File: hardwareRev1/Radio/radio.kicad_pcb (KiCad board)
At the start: 4 copper layers, 37 x 24.5 mm, 61 parts, among them J1 SMA, U1 AX503, U2 PE42424, U3 RF5110G, X1 TCXO

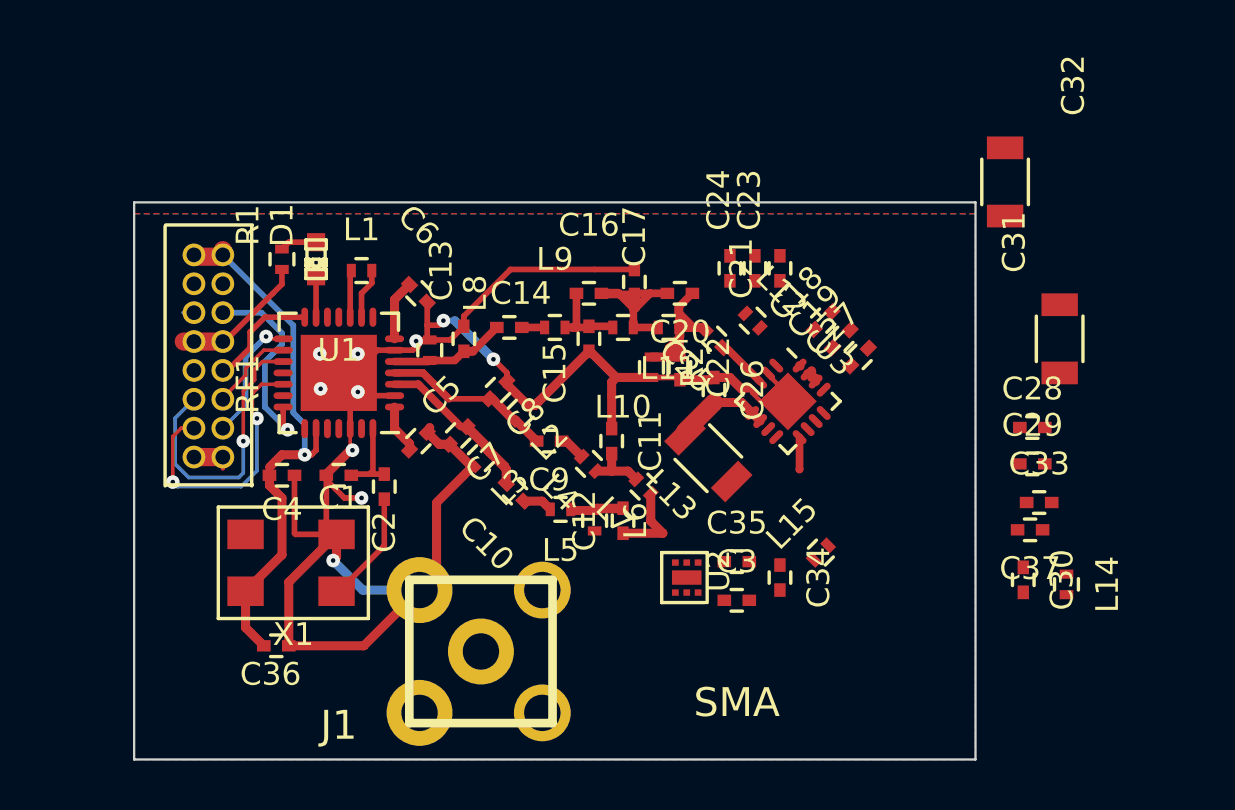
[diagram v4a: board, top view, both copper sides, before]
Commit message: Made the board 4 layer.
Added a MCU to theback...
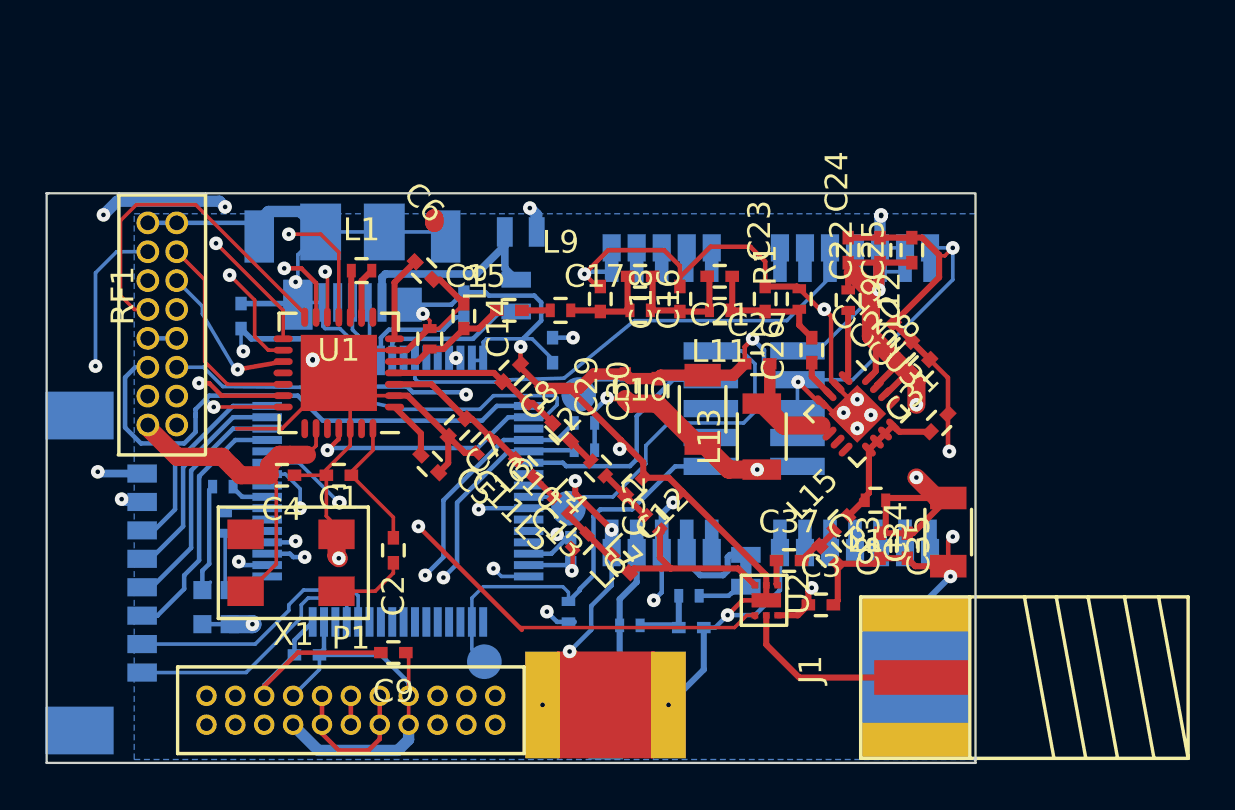
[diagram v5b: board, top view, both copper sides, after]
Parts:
- added C38: C, Capacitors_SMD:C_0402, B.Cu at (81.5, 57.0)
- added C39: C, Capacitors_SMD:C_0402, B.Cu at (71.7, 57.5)
- added C40: C, Capacitors_SMD:C_0402, B.Cu at (74.6, 72.4)
- added C41: C, Capacitors_SMD:C_0402, B.Cu at (86.2, 67.8)
- added C42: C, Capacitors_SMD:C_0402, B.Cu at (85.4, 59.0)
- added C43: 47pF, Capacitors_SMD:C_0402, B.Cu at (91.5, 71.2)
- added D2: LED, LEDs:LED-0603, B.Cu at (71.2, 70.3)
- added J2: edgeMountSMA, hardwareRev1:EdgeSMA, B.Cu at (90.5, 78.6)
- added JMP2: SJMPClosed, SMDJMP-CLOSED, B.Cu at (93.9, 68.7)
- added JMP3: SJMPOpen, hardwareRev1:SMDJMP-OPEN, B.Cu at (84.0, 53.8)
- added JMP4: SJMPOpen, hardwareRev1:SMDJMP-OPEN, B.Cu at (83.8, 56.6)
- added L16: 27nH, Resistors_SMD:R_0402, B.Cu at (88.8, 71.1)
- added P1: CONN_11X2, hardwareRev1:1.27mmPitchHeader11X2, F.Cu at (77.8, 74.2)
- added P2: CONN_1, Measurement_Points:Measurement_Point_Round-SMD-Pad_Small, B.Cu at (86.1, 66.0)
- added P3: CONN_8, Connectors_Molex:Connector_Molex_PicoBlade_53398-0871, B.Cu at (64.6, 68.8)
- added P4: CONN_5X2, hardwareRev1:CortexDebug, B.Cu at (94.9, 60.3)
- added P5: CONN_1, Measurement_Points:Measurement_Point_Round-SMD-Pad_Small, B.Cu at (86.5, 61.0)
- added P6: CONN_1, Measurement_Points:Measurement_Point_Round-SMD-Pad_Small, B.Cu at (82.4, 72.7)
- added R3: R, Resistors_SMD:R_0402, B.Cu at (86.8, 62.2)
- added R4: R, Resistors_SMD:R_0402, B.Cu at (70.9, 65.0)
- added R5: R, Resistors_SMD:R_0402, B.Cu at (71.0, 66.6)
- added R6: R, Resistors_SMD:R_0402, B.Cu at (86.1, 70.5)
- added R7: 10, Resistors_SMD:R_0402, B.Cu at (91.4, 69.8)
- added RF2: NEO7, NEO-7, B.Cu at (87.0, 54.5)
- added U4: MKL26Z128VLH4, w_smd_lqfp:lqfp64, B.Cu at (78.6, 65.2)
- added U6: MICRO-B_USB, USB:USB micro-female, B.Cu at (76.6, 54.0)
- C11: value 12pf -> 10pf
- C13: value 2.2pf -> 12pf
- C14: value 22pf -> 2.2pf
- C15: value 33pf -> 22pf
- C16: value 4.7pf -> 33pf
- C17: value 47pf -> 4.7pf
- C18: value 10nf -> 47pf
- C19: value 1nf -> 10nf
- C20: value 1.8pf -> 1nf
- C21: value 10nf -> 1.8pf
- C22: value 15pf -> 10nf
- C23: value 1nf -> 15pf
- C24: value 27pf -> 1nf
- C25: value 100pf -> 27pf
- C26: value 27pf -> 100pf
- C27: value 47pf -> 27pf
- C28: value 1nf -> 47pf
- C29: value 10nf -> 1nf
- C30: value 33pf -> 10nf
- C31: value 3.3uf -> 33pf; footprint Capacitors_SMD:C_1206 -> Capacitors_SMD:C_0402
- C33: value 1nf -> C
- C34: value 56pf -> 3.3uf; footprint Capacitors_SMD:C_0402 -> Capacitors_SMD:C_1206
- C35: value 100pf -> 1nf
- C36: value 100pf -> 56pf
- C37: value C -> 100pf
- C9: value 10pf -> 100pf
- D1: moved to B.Cu
- J1: value SMA -> edgeMountSMA; footprint hardwareRev1:SMA -> hardwareRev1:EdgeSMA
- R1: value R -> 180
- R2: value 180 -> R; moved to B.Cu
- RF1: footprint 1.27mm2X8 -> hardwareRev1:1.27mm2X8
- U2: footprint PE4242 -> hardwareRev1:PE4242
- X1: footprint FOX924B -> hardwareRev1:FOX924B
- moved C36 24.6 mm to (97.5, 68.0), turned to 315 degrees
- moved J1 23.4 mm to (105.3, 76.2), turned to 90 degrees
- moved R1 22.8 mm to (96.2, 56.8)
- moved C29 18.2 mm to (88.6, 60.6), turned to 90 degrees
- moved C30 18.1 mm to (90.0, 60.8), turned to 90 degrees
- moved C32 16.6 mm to (92.0, 61.6), turned to 90 degrees
- moved D1 16.1 mm to (70.0, 70.3), turned to 270 degrees
- moved C13 12.1 mm to (88.4, 68.4), turned to 135 degrees
- moved C9 11.6 mm to (78.4, 72.3)
- moved RF1 10.8 mm to (67.6, 53.4), turned to 180 degrees
- moved C37 10.7 mm to (95.8, 68.2), turned to 0 degrees
- moved C22 10.2 mm to (99.8, 54.6), turned to 90 degrees
- moved C20 10.1 mm to (100.8, 59.0), turned to 45 degrees
- moved C25 9.53 mm to (101.2, 54.6), turned to 90 degrees
- moved L14 9.18 mm to (99.6, 65.6), turned to 180 degrees
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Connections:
- C11 pad 1: GND -> Net-(C11-Pad1)
- C12 pad 1: Net-(C12-Pad1) -> GND
- C13 pad 1: /PA/PAInput -> Net-(C13-Pad1)
- C13 pad 2: GND -> Net-(C13-Pad2)
- C14 pad 1: Net-(C14-Pad1) -> /PA/PAInput
- C14 pad 2: /PA/PAInput -> GND
- C15 pad 2: GND -> /PA/PAInput
- C16 pad 2: Net-(C15-Pad1) -> GND
- C17 pad 1: Net-(C16-Pad1) -> Net-(C17-Pad1)
- C17 pad 2: GND -> Net-(C16-Pad1)
- C18 pad 1: +3.3V -> Net-(C17-Pad1)
- C20 pad 1: Net-(C20-Pad1) -> +3.3V
- C20 pad 2: Net-(C16-Pad1) -> GND
- C21 pad 1: +3.3V -> Net-(C21-Pad1)
- C21 pad 2: GND -> Net-(C17-Pad1)
- C22 pad 1: Net-(C20-Pad1) -> +3.3V
- C23 pad 1: +3.3V -> Net-(C21-Pad1)
- C25 pad 1: Net-(C25-Pad1) -> +3.3V
- C25 pad 2: Net-(C20-Pad1) -> GND
- C26 pad 1: GND -> Net-(C26-Pad1)
- C26 pad 2: Net-(C26-Pad2) -> Net-(C21-Pad1)
- C27 pad 1: +3.3V -> GND
- C27 pad 2: GND -> Net-(C27-Pad2)
- C30 pad 1: Net-(C30-Pad1) -> +3.3V
- C31 pad 1: +3.3V -> Net-(C31-Pad1)
- C32 pad 1: GND -> +3.3V
- C32 pad 2: +3.3V -> GND
- C33 pad 1: +3.3V -> GND
- C33 pad 2: GND -> +3.3V
- C34 pad 1: Net-(C34-Pad1) -> GND
- C34 pad 2: GND -> +3.3V
- C35 pad 1: /PA/PAOutput -> +3.3V
- C35 pad 2: Net-(C34-Pad1) -> GND
- C36 pad 1: GND -> Net-(C36-Pad1)
- C36 pad 2: +3.3V -> GND
- C37 pad 1: GND -> /PA/PAOutput
- C37 pad 2: +3.3V -> Net-(C36-Pad1)
- C7 pad 1: Net-(C10-Pad2) -> Net-(C11-Pad2)
- C8 pad 2: Net-(C8-Pad2) -> Net-(C10-Pad2)
- C9 pad 1: Net-(C9-Pad1) -> GND
- C9 pad 2: Net-(C8-Pad2) -> +3.3V
- D1 pad 2: Net-(D1-Pad2) -> GND
- L10 pad 1: Net-(C16-Pad1) -> Net-(C17-Pad1)
- L10 pad 2: Net-(C15-Pad1) -> Net-(C16-Pad1)
- L11 pad 1: Net-(C20-Pad1) -> Net-(C21-Pad1)
- L11 pad 2: Net-(C16-Pad1) -> Net-(C17-Pad1)
- L13 pad 2: Net-(C26-Pad2) -> Net-(C27-Pad2)
- L14 pad 2: Net-(C30-Pad1) -> Net-(C31-Pad1)
- L15 pad 1: Net-(C34-Pad1) -> Net-(C36-Pad1)
- L15 pad 2: Net-(C30-Pad1) -> Net-(C31-Pad1)
- L2 pad 2: Net-(C8-Pad2) -> Net-(C10-Pad2)
- L3 pad 1: Net-(C10-Pad2) -> Net-(C11-Pad2)
- L4 pad 1: Net-(C11-Pad2) -> Net-(C12-Pad2)
- L4 pad 2: Net-(C9-Pad1) -> Net-(C10-Pad1)
- L5 pad 1: Net-(C12-Pad2) -> Net-(C13-Pad2)
- L5 pad 2: Net-(C10-Pad1) -> Net-(C11-Pad1)
- L6 pad 1: Net-(C12-Pad2) -> Net-(C13-Pad2)
- L7 pad 1: Net-(C12-Pad1) -> Net-(C13-Pad1)
- L7 pad 2: Net-(C11-Pad2) -> Net-(C12-Pad2)
- L9 pad 1: Net-(C15-Pad1) -> Net-(C16-Pad1)
- L9 pad 2: Net-(C14-Pad1) -> Net-(C15-Pad1)
- R1 pad 1: GND -> Net-(C21-Pad1)
- R1 pad 2: Net-(D1-Pad2) -> GND
- R2 pad 1: Net-(C20-Pad1) -> +3.3V
- R2 pad 2: GND -> /internalI2C0SDA
- U1 pad 12: (no net) -> /DataCLK
- U1 pad 13: Net-(D1-Pad1) -> /CLKOut
- U1 pad 3: Net-(C10-Pad2) -> Net-(C11-Pad2)
- U1 pad 4: Net-(C8-Pad2) -> Net-(C10-Pad2)
- U2 pad 6: Net-(C12-Pad1) -> Net-(C13-Pad1)
- U3 pad 10: Net-(C30-Pad1) -> Net-(C31-Pad1)
- U3 pad 11: Net-(C30-Pad1) -> Net-(C31-Pad1)
- U3 pad 12: Net-(C30-Pad1) -> Net-(C31-Pad1)
- U3 pad 3: Net-(C25-Pad1) -> Net-(C26-Pad1)
- U3 pad 5: Net-(C26-Pad2) -> Net-(C27-Pad2)
- U3 pad 6: Net-(C26-Pad2) -> Net-(C27-Pad2)
- U3 pad 9: Net-(C30-Pad1) -> Net-(C31-Pad1)
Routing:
- net GND: track 94.6 -> 298.4 mm, vias 10 -> 30
- net +3.3V: track 25.4 -> 185.4 mm, vias 1 -> 15
- net /USBV1: track 0.00 -> 61.5 mm, vias 0 -> 3
- net /TXRX: track 0.00 -> 35.4 mm, vias 0 -> 2
- net /MISO: track 3.80 -> 34.4 mm, vias 0 -> 2
- net /AF_IN: track 0.48 -> 29.9 mm, vias 0 -> 1
- net /DATA: track 0.00 -> 28.8 mm, vias 0 -> 3
- net /CLK: track 5.61 -> 32.8 mm, vias 1 -> 3
- net /internalI2C0SDA: track 0.00 -> 22.6 mm, vias 0 -> 1
- net /CLKOut: track 0.00 -> 22.4 mm, vias 0 -> 2
- net /GPSTX: track 0.00 -> 22.1 mm
- net /internalI2C0SCL: track 0.00 -> 18.7 mm, vias 0 -> 1
- net /IRQOUT: track 12.6 -> 31.1 mm, vias 2 -> 1
- net /AF_OUT: track 9.03 -> 27.5 mm
- net /SWD_CLK: track 0.00 -> 18.5 mm
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- added copper zone on In2.Cu, net +3.3V
- added copper zone on In1.Cu, net GND
- removed copper zone on F.Cu, net GND
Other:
- board size 37 x 24.5 mm -> 40.9 x 25.1 mm
- net class Default: clearance 0.1524 -> 0.127
- rule trace_clearance: 0.1524 -> 0.127

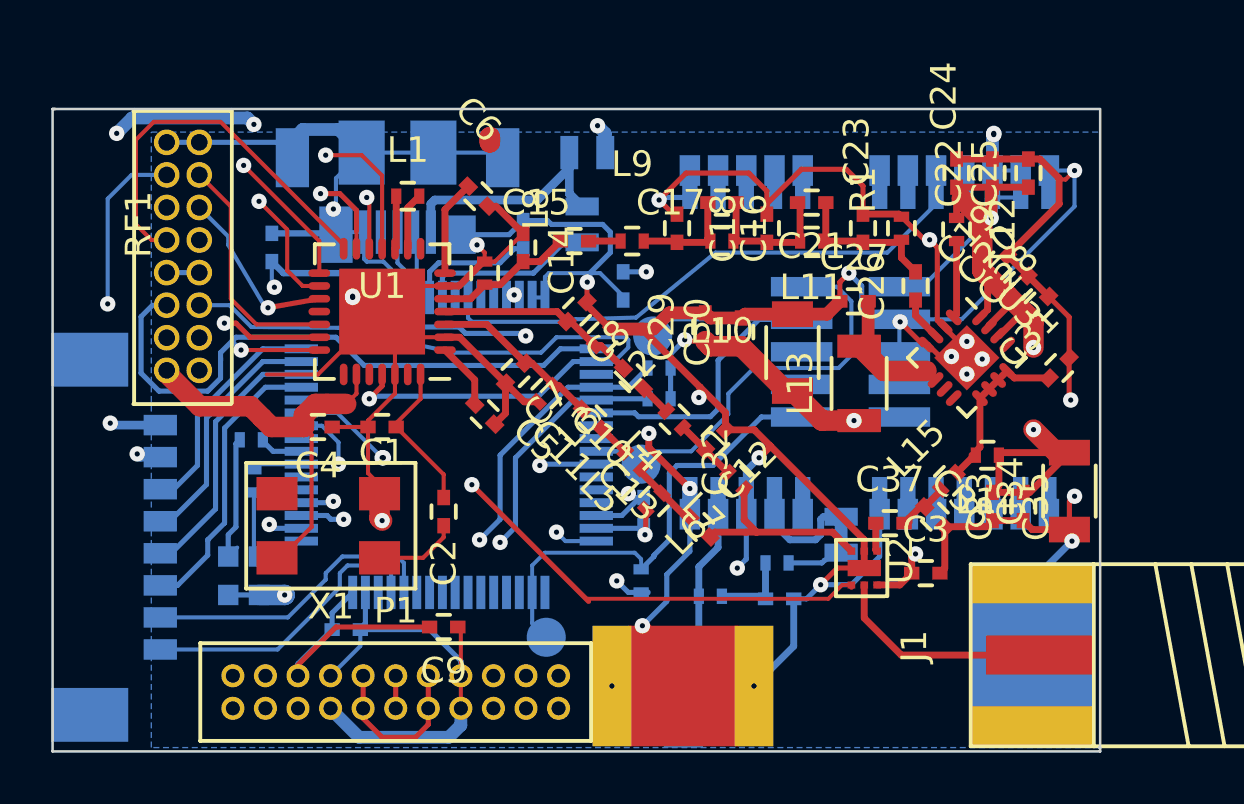
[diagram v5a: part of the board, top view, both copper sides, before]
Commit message: Modified the radio according to John. Should be almost good to go.
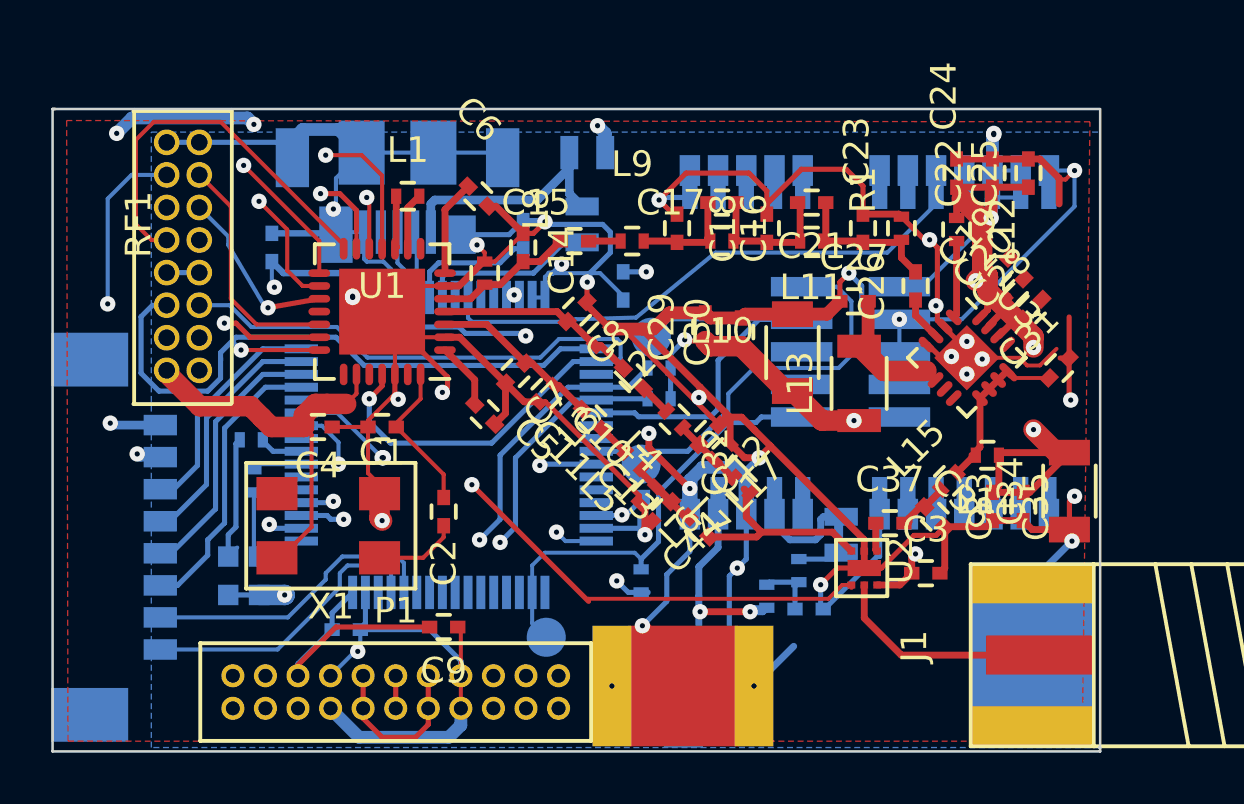
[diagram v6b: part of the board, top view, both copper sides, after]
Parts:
- added C44: C, Capacitors_SMD:C_0402, F.Cu at (86.9, 67.8)
- added L17: INDUCTOR, Resistors_SMD:R_0402, F.Cu at (89.2, 65.5)
- moved L16 2.20 mm to (91.0, 71.1), turned to 90 degrees
- moved C43 1.22 mm to (92.7, 71.6)
- moved R7 0.90 mm to (92.2, 70.1), turned to 270 degrees
- moved L6 0.35 mm to (86.3, 67.2)
- moved C12 0.32 mm to (88.8, 64.8)
- moved L7 0.29 mm to (90.0, 66.8)
- moved C28 0.28 mm to (101.3, 59.9)
- moved C20 0.20 mm to (100.6, 59.1)
- moved C19 0.11 mm to (100.0, 58.3)
- moved P5 0.07 mm to (86.5, 61.0)
- moved C13 0.05 mm to (88.3, 68.4)
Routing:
- net GND: track 298.4 -> 317.0 mm, vias 30 -> 36
- net Net-(J2-Pad1): track 8.56 -> 11.9 mm, vias 0 -> 2
- net /AF_IN: track 29.9 -> 32.7 mm
- net +3.3V: track 185.4 -> 184.6 mm, vias 15 -> 16
- net Net-(C13-Pad2): track 2.77 -> 3.63 mm
- net Net-(C43-Pad1): track 3.14 -> 2.40 mm
- net Net-(JMP2-Pad1): track 5.69 -> 4.97 mm
- net Net-(JMP2-Pad2): track 1.44 -> 2.04 mm
- net /SWD_Reset: track 18.3 -> 17.7 mm
- added copper zone on F.Cu, net GND
